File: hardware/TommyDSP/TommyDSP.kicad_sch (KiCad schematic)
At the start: 0 parts

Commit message: add Microcontroller circuit
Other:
- added sheet MCU-Core (MCU-Core.kicad_sch)
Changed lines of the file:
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@@
 	(generator_version "9.0")
 	(paper "A4")
+	(sheet
+		(at 25.4 25.4)
+		(size 38.1 88.9)
+		(exclude_from_sim no)
+		(in_bom yes)
+		(on_board yes)
+		(dnp no)
+		(fields_autoplaced yes)
+		(stroke
+			(width 0.1524)
+			(type solid)
+		)
+		(fill
+			(color 0 0 0 0.0000)
+		)
+		(property "Sheetname" "MCU-Core"
+			(at 25.4 24.6884 0)
+			(effects
+				(font
+					(size 1.27 1.27)
+				)
+				(justify left bottom)
+			)
+		)
+		(property "Sheetfile" "MCU-Core.kicad_sch"
+			(at 25.4 114.8846 0)
+			(effects
+				(font
+					(size 1.27 1.27)
+				)
+				(justify left top)
+			)
+		)
+		(instances
+			(project "TommyDSP"
+				(path "/8e0e2dd5-fa84-4cc4-affc-8a947fbe8a29"
+					(page "2")
+				)
+			)
+		)
+	)
 	(sheet_instances
 		(path "/"

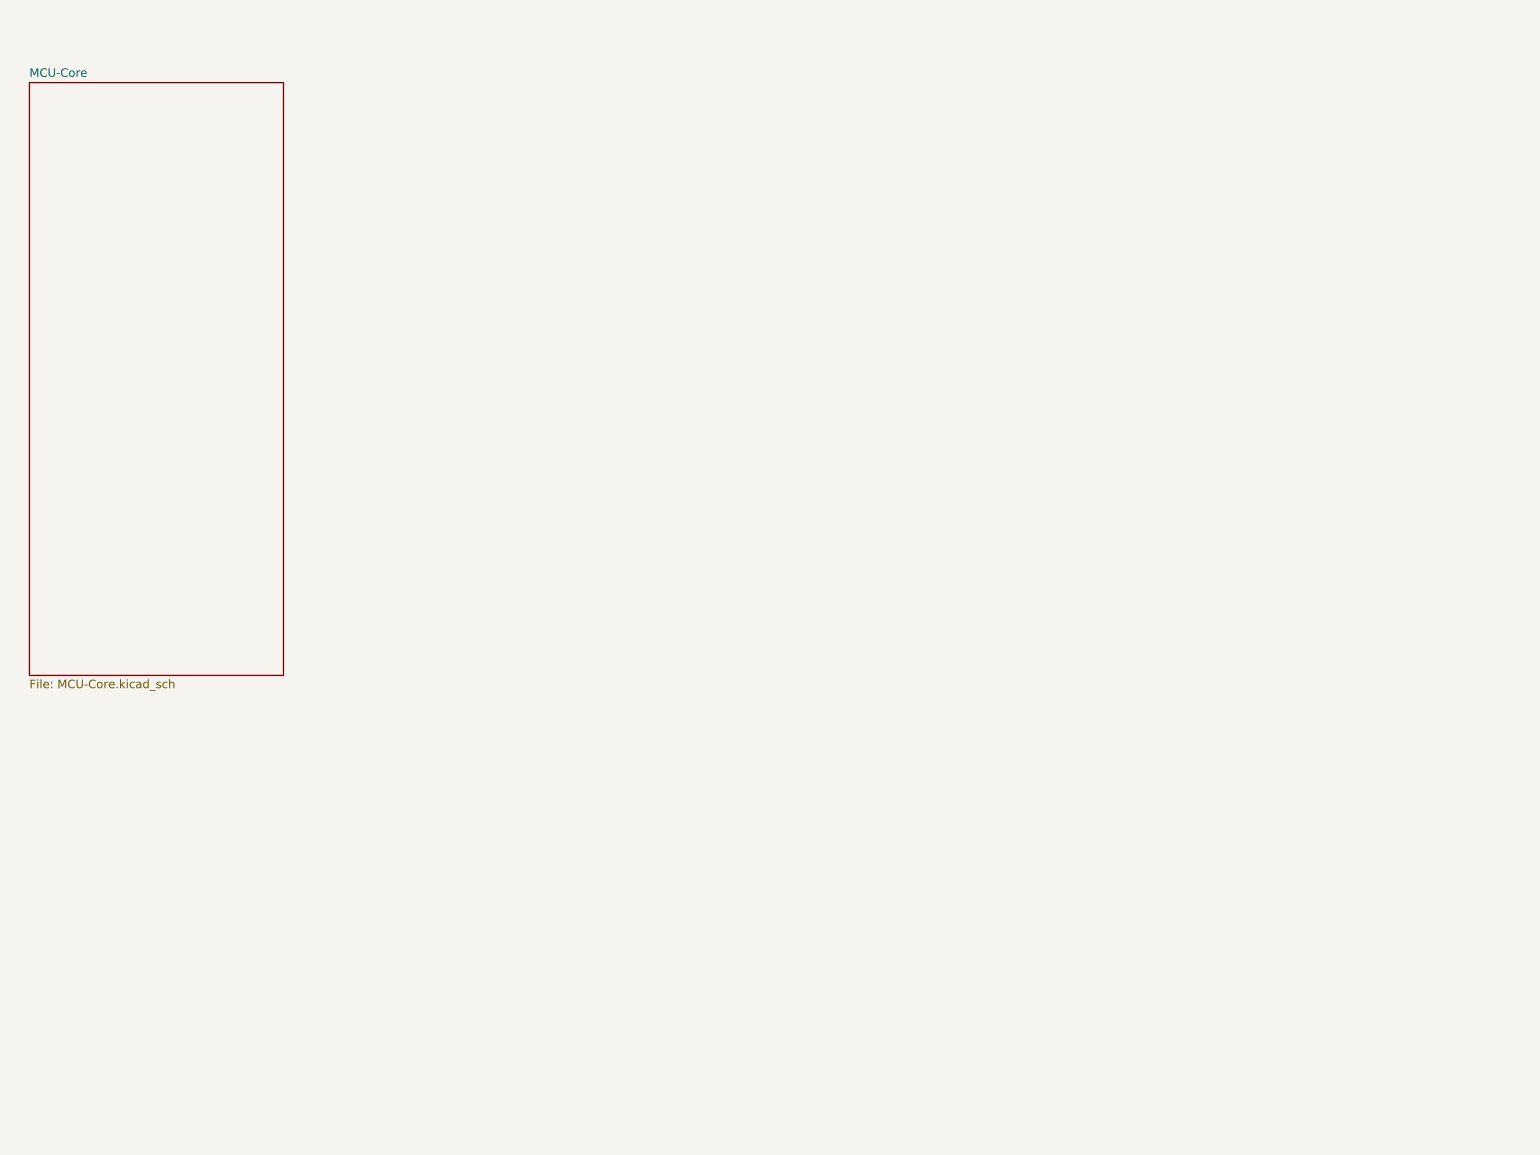
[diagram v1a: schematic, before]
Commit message: hardware: finished PCB routing
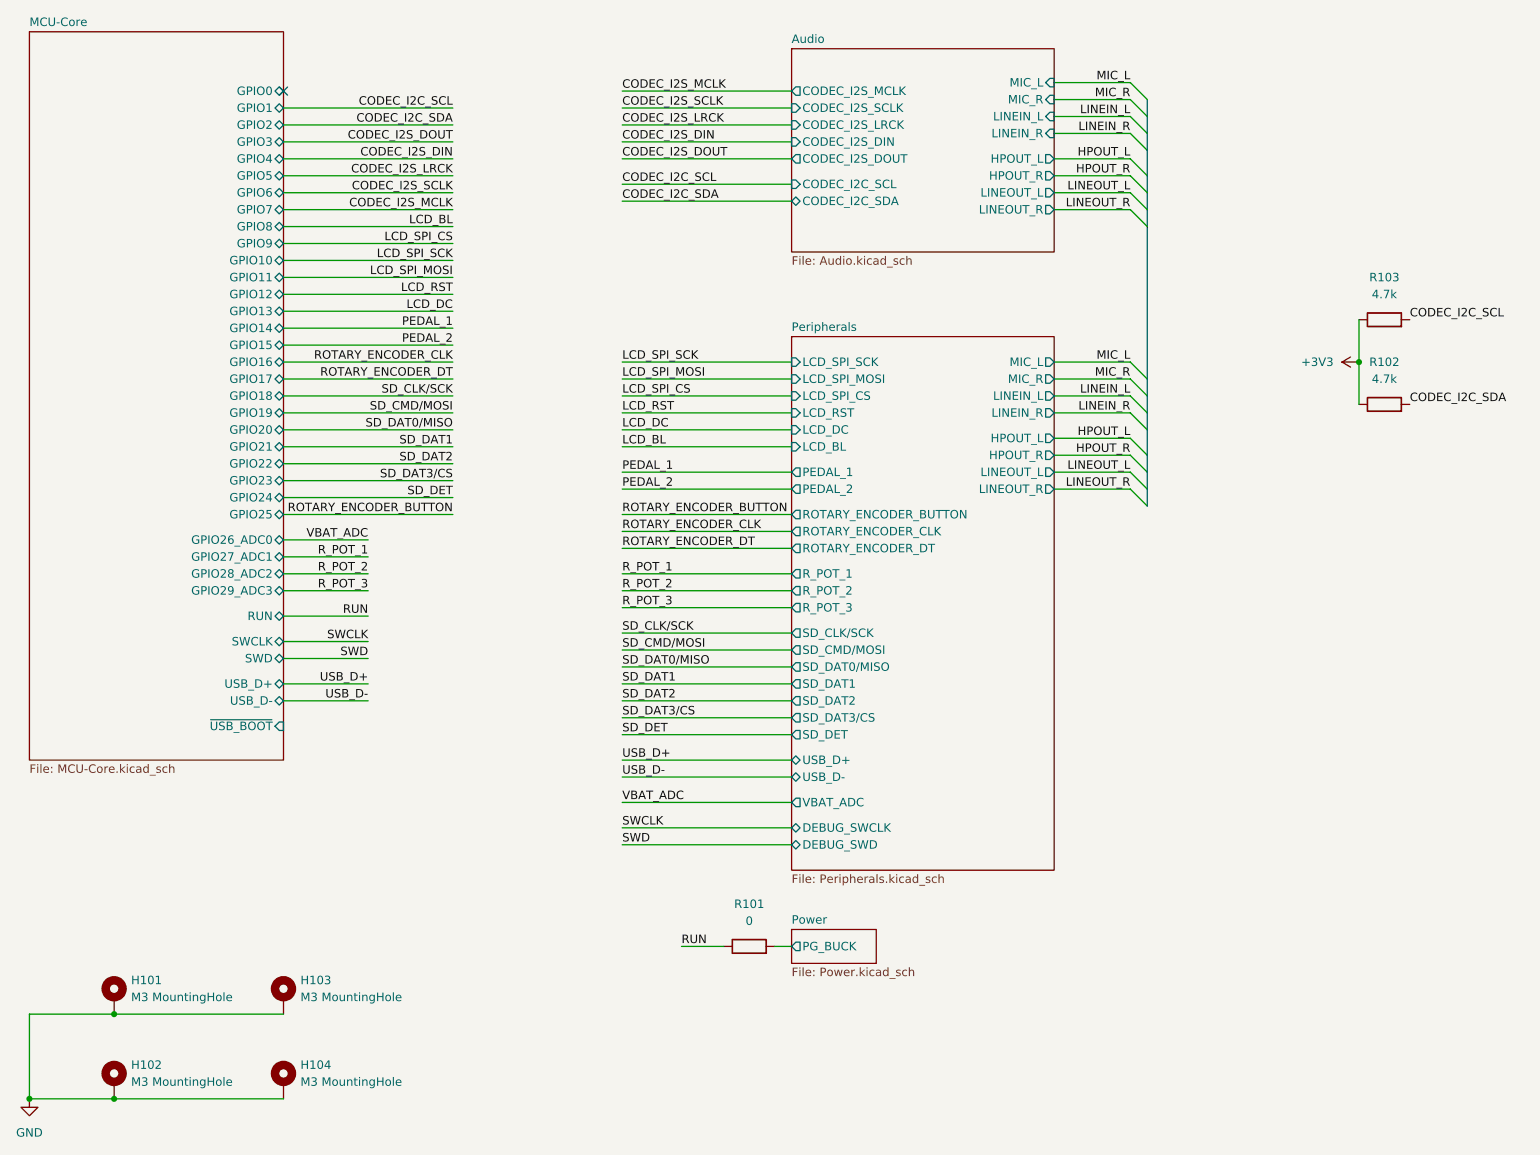
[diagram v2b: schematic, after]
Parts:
- added H101, H102, H103, H104: M3 MountingHole, MountingHole:MountingHole_3.2mm_M3_DIN965_Pad_TopBottom, symbol Mechanical:MountingHole_Pad
- added R101: 0, Resistor_SMD:R_0603_1608Metric, symbol Device:R
- added R102, R103: 4.7k, Resistor_SMD:R_0603_1608Metric, symbol Device:R
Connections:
- new net +3V3: R102.1, R103.1
- new net CODEC_I2C_SCL: R103.2
- new net CODEC_I2C_SDA: R102.2
- new net GND: H101.1, H102.1, H103.1, H104.1
- new net Power/PG_BUCK: R101.2
- new net RUN: R101.1
- no-connect marks 0 -> 1
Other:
- added sheet Audio (Audio.kicad_sch)
- added sheet Peripherals (Peripherals.kicad_sch)
- added sheet Power (Power.kicad_sch)
- sheet MCU-Core ports: added GPIO0, GPIO1, GPIO10, GPIO11, GPIO12, GPIO13, GPIO14, GPIO15, GPIO16, GPIO17, GPIO18, GPIO19, GPIO2, GPIO20, GPIO21, GPIO22, GPIO23, GPIO24, GPIO25, GPIO26_ADC0, GPIO27_ADC1, GPIO28_ADC2, GPIO29_ADC3, GPIO3, GPIO4, GPIO5, GPIO6, GPIO7, GPIO8, GPIO9, RUN, SWCLK, SWD, USB_D+, USB_D-, ~{USB_BOOT}; removed none
- title: (none) -> TommyDSP

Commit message: hardware: finalize PCB design
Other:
- sheet Peripherals ports: added I2C_SCL, I2C_SDA; removed none
- moved on the sheet: R101
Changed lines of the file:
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@@
 	(wire
 		(pts
+			(xy 114.3 129.54) (xy 139.7 129.54)
+		)
+		(stroke
+			(width 0)
+			(type default)
+		)
+	)
+	(wire
+		(pts
 			(xy 114.3 67.31) (xy 139.7 67.31)
 		)
@@
 	(wire
 		(pts
-			(xy 123.19 154.94) (xy 129.54 154.94)
+			(xy 123.19 167.64) (xy 129.54 167.64)
 		)
 		(stroke
@@
 	(wire
 		(pts
-			(xy 114.3 139.7) (xy 139.7 139.7)
+			(xy 114.3 146.05) (xy 139.7 146.05)
 		)
 		(stroke
@@
 	(wire
 		(pts
-			(xy 137.16 154.94) (xy 139.7 154.94)
+			(xy 137.16 167.64) (xy 139.7 167.64)
 		)
 		(stroke
@@
 	(wire
 		(pts
-			(xy 114.3 127) (xy 139.7 127)
+			(xy 114.3 133.35) (xy 139.7 133.35)
 		)
 		(stroke
@@
 	(wire
 		(pts
-			(xy 114.3 129.54) (xy 139.7 129.54)
+			(xy 114.3 135.89) (xy 139.7 135.89)
 		)
 		(stroke
@@
 	(wire
 		(pts
-			(xy 114.3 133.35) (xy 139.7 133.35)
+			(xy 114.3 139.7) (xy 139.7 139.7)
 		)
 		(stroke
@@
 	(wire
 		(pts
-			(xy 114.3 137.16) (xy 139.7 137.16)
+			(xy 114.3 143.51) (xy 139.7 143.51)
 		)
 		(stroke
@@
 	(wire
 		(pts
+			(xy 114.3 127) (xy 139.7 127)
+		)
+		(stroke
+			(width 0)
+			(type default)
+		)
+	)
+	(wire
+		(pts
 			(xy 63.5 77.47) (xy 88.9 77.47)
 		)
@@
 	)
 	(label "SWD"
-		(at 114.3 139.7 0)
+		(at 114.3 146.05 0)
 		(effects
 			(font
@@
 		)
 	)
-	(label "CODEC_I2C_SDA"
+	(label "I2C_SDA"
 		(at 88.9 31.75 180)
 		(effects
@@
 	)
 	(label "RUN"
-		(at 123.19 154.94 0)
+		(at 123.19 167.64 0)
 		(effects
 			(font
@@
 	)
 	(label "VBAT_ADC"
-		(at 114.3 133.35 0)
+		(at 114.3 139.7 0)
 		(effects
 			(font
@@
 	)
 	(label "USB_D-"
-		(at 114.3 129.54 0)
+		(at 114.3 135.89 0)
 		(effects
 			(font
@@
 	)
 	(label "USB_D+"
-		(at 114.3 127 0)
+		(at 114.3 133.35 0)
 		(effects
 			(font
@@
 	)
 	(label "SWCLK"
-		(at 114.3 137.16 0)
+		(at 114.3 143.51 0)
 		(effects
 			(font
@@
 		)
 	)
+	(label "CODEC_I2C_SCL"
+		(at 114.3 127 0)
+		(effects
+			(font
+				(size 1.27 1.27)
+			)
+			(justify left bottom)
+		)
+	)
 	(label "CODEC_I2S_MCLK"
 		(at 88.9 44.45 180)
@@
 		)
 	)
-	(label "CODEC_I2C_SCL"
+	(label "I2C_SCL"
 		(at 88.9 29.21 180)
 		(effects
@@
 		)
 	)
+	(label "CODEC_I2C_SDA"
+		(at 114.3 129.54 0)
+		(effects
+			(font
+				(size 1.27 1.27)
+			)
+			(justify left bottom)
+		)
+	)
 	(label "CODEC_I2S_LRCK"
 		(at 114.3 31.75 0)
@@
 	(symbol
 		(lib_id "Device:R")
-		(at 133.35 154.94 90)
+		(at 133.35 167.64 90)
 		(unit 1)
 		(exclude_from_sim no)
@@
 		(fields_autoplaced yes)
 		(property "Reference" "R101"
-			(at 133.35 148.59 90)
+			(at 133.35 161.29 90)
 			(effects
 				(font
@@
 		)
 		(property "Value" "0"
-			(at 133.35 151.13 90)
+			(at 133.35 163.83 90)
 			(effects
 				(font
@@
 		)
 		(property "Footprint" "Resistor_SMD:R_0603_1608Metric"
-			(at 133.35 156.718 90)
+			(at 133.35 169.418 90)
 			(effects
 				(font
@@
 		)
 		(property "Datasheet" "~"
-			(at 133.35 154.94 0)
+			(at 133.35 167.64 0)
 			(effects
 				(font
@@
 		)
 		(property "Description" "Resistor"
-			(at 133.35 154.94 0)
+			(at 133.35 167.64 0)
 			(effects
 				(font
@@
 	(sheet
 		(at 139.7 63.5)
-		(size 39.37 80.01)
+		(size 39.37 90.17)
 		(exclude_from_sim no)
 		(in_bom yes)
@@
 		)
 		(property "Sheetfile" "Peripherals.kicad_sch"
-			(at 139.7 144.0946 0)
+			(at 139.7 154.2546 0)
 			(effects
 				(font
@@
 		)
 		(pin "DEBUG_SWCLK" bidirectional
-			(at 139.7 137.16 180)
+			(at 139.7 143.51 180)
 			(effects
 				(font
@@
 		)
 		(pin "DEBUG_SWD" bidirectional
-			(at 139.7 139.7 180)
+			(at 139.7 146.05 180)
 			(effects
 				(font
@@
 		)
 		(pin "USB_D+" bidirectional
-			(at 139.7 127 180)
+			(at 139.7 133.35 180)
 			(effects
 				(font
@@
 		)
 		(pin "USB_D-" bidirectional
-			(at 139.7 129.54 180)
+			(at 139.7 135.89 180)
 			(effects
 				(font
@@
 		)
 		(pin "VBAT_ADC" output
-			(at 139.7 133.35 180)
+			(at 139.7 139.7 180)
+			(effects
+				(font
+					(size 1.27 1.27)
+				)
+				(justify left)
+			)
+		)
+		(pin "I2C_SCL" input
+			(at 139.7 127 180)
+			(effects
+				(font
+					(size 1.27 1.27)
+				)
+				(justify left)
+			)
+		)
+		(pin "I2C_SDA" bidirectional
+			(at 139.7 129.54 180)
 			(effects
 				(font
@@
 	)
 	(sheet
-		(at 139.7 152.4)
+		(at 139.7 165.1)
 		(size 12.7 5.08)
 		(exclude_from_sim no)
@@
 		)
 		(property "Sheetname" "Power"
-			(at 139.7 151.6884 0)
+			(at 139.7 164.3884 0)
 			(effects
 				(font
@@
 		)
 		(property "Sheetfile" "Power.kicad_sch"
-			(at 139.7 158.0646 0)
+			(at 139.7 170.7646 0)
 			(effects
 				(font
@@
 		)
 		(pin "PG_BUCK" output
-			(at 139.7 154.94 180)
+			(at 139.7 167.64 180)
 			(effects
 				(font

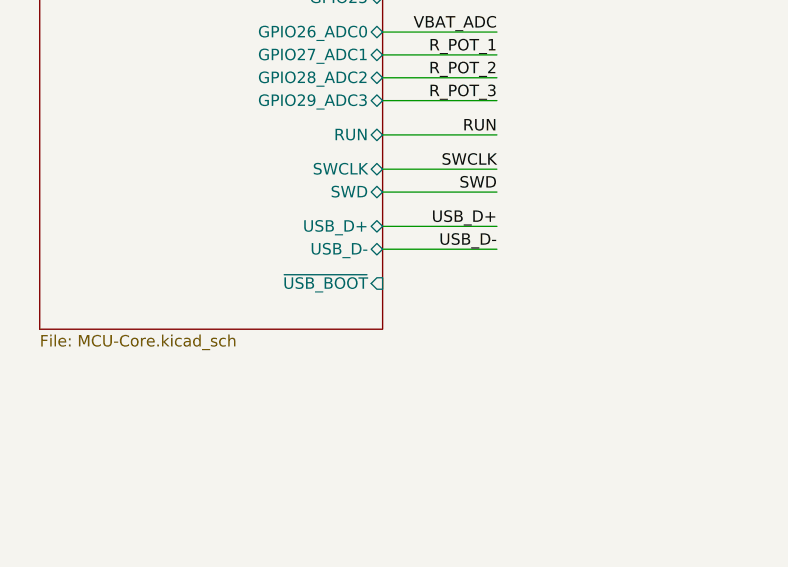
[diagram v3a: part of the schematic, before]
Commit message: hardware: adjust value of BUCK feedback resistors
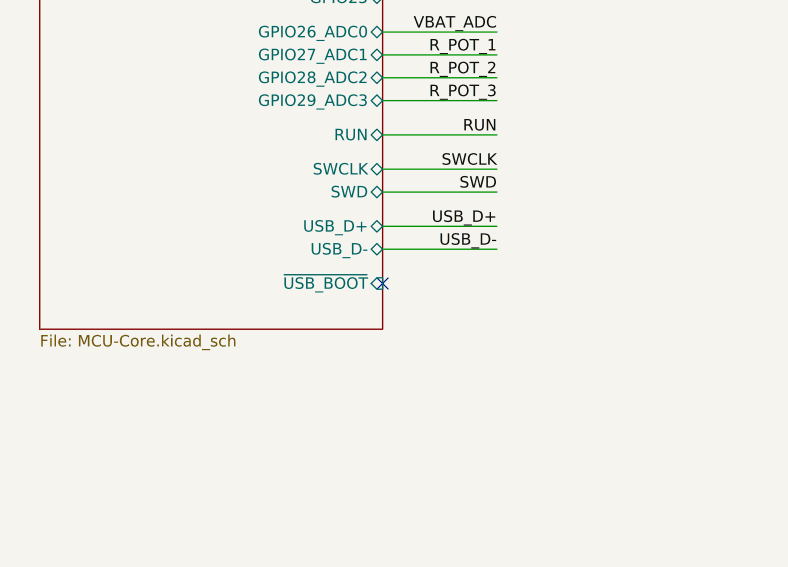
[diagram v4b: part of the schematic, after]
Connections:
- no-connect marks 1 -> 2
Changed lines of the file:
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@@
+	)
+	(no_connect
+		(at 63.5 121.92)
 	)
 	(no_connect
